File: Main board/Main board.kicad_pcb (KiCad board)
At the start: 2 copper layers, 126 x 88.5 mm, 35 parts

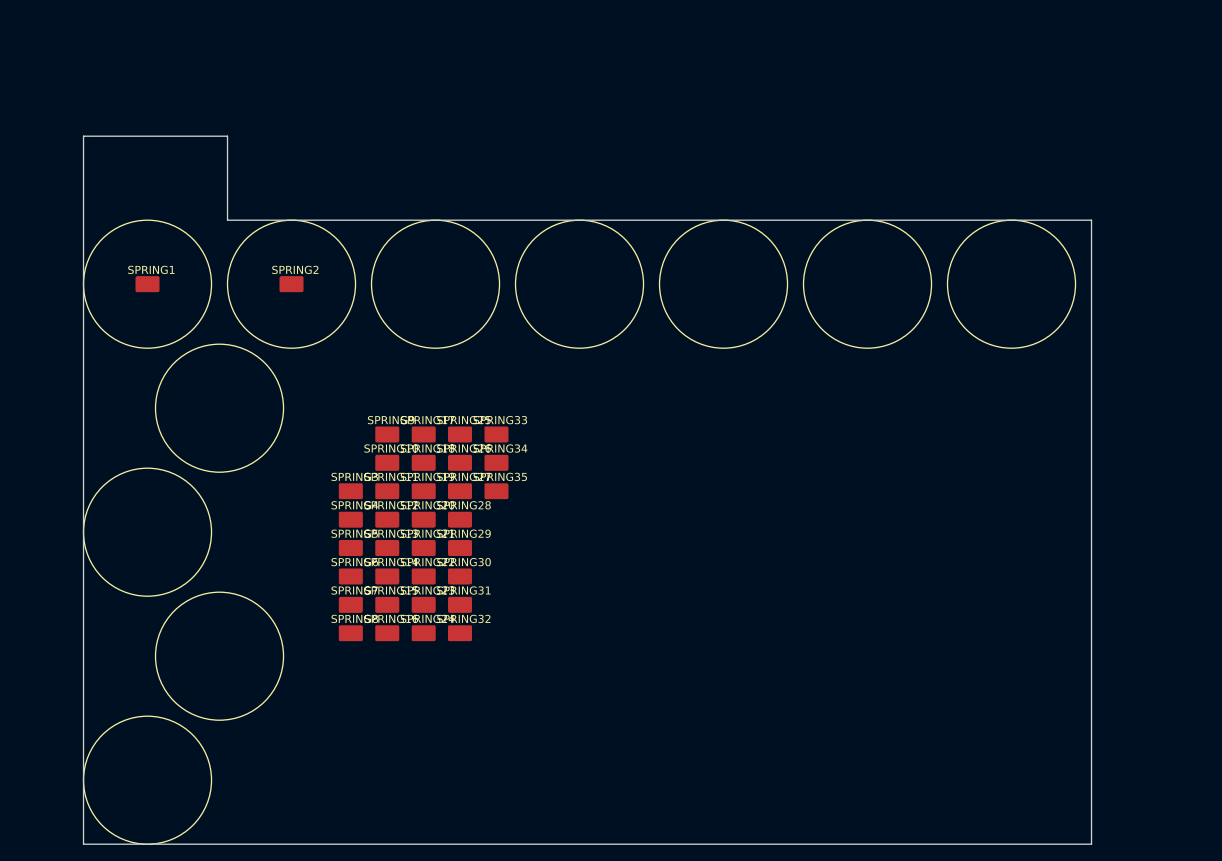
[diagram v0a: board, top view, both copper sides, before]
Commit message: Created breakable symmetrical version
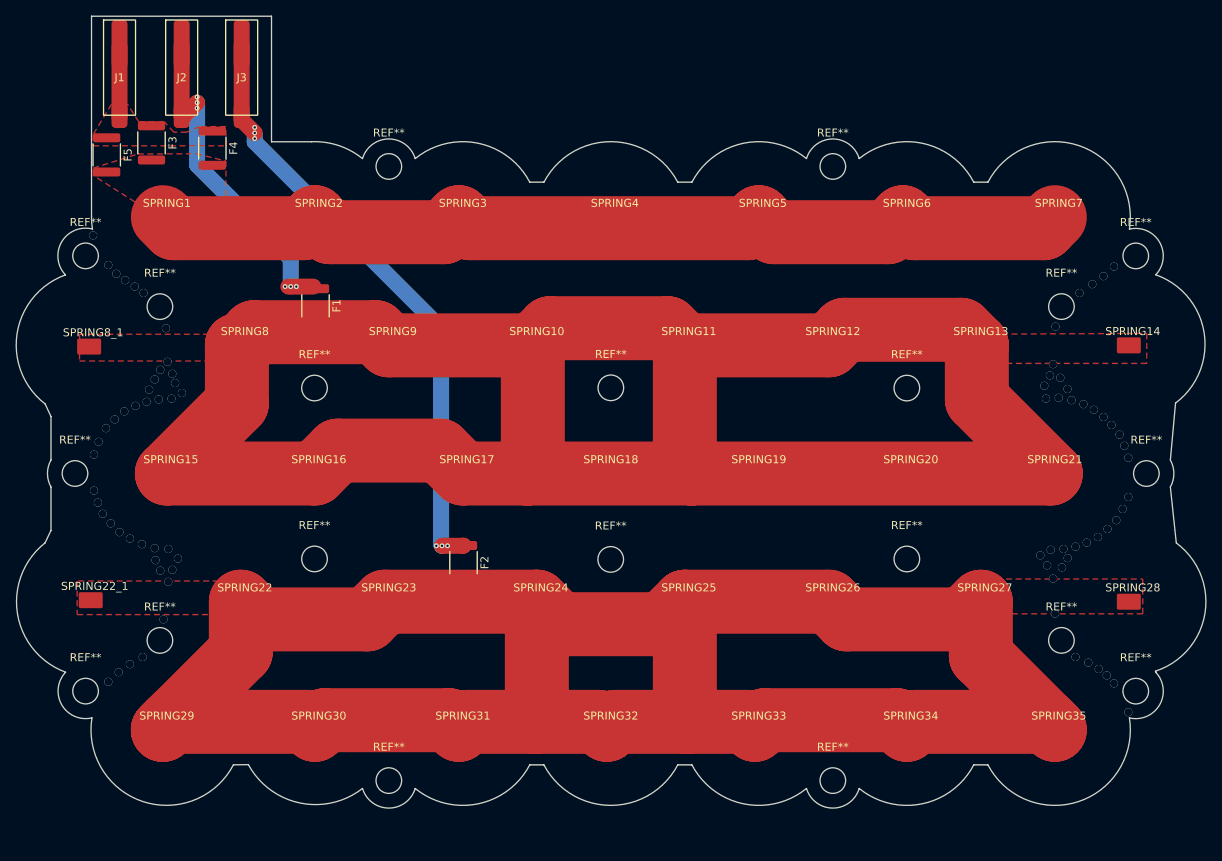
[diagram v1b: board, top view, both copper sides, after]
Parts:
- added F1: Polyfuse, Fuse:Fuse_1812_4532Metric, F.Cu at (41.0, 33.2)
- added F2: Polyfuse, Fuse:Fuse_1812_4532Metric, F.Cu at (59.5, 65.3)
- added F3: Polyfuse, Fuse:Fuse_1812_4532Metric, F.Cu at (20.5, 12.8)
- added F4: Polyfuse, Fuse:Fuse_1812_4532Metric, F.Cu at (28.1, 13.5)
- added F5: Polyfuse, Fuse:Fuse_1812_4532Metric, F.Cu at (14.9, 14.3)
- added J1: Conn_01x01_Pin, SMD_spring_clamp_connector:SMD_spring_clamp_connector_1x1, F.Cu at (16.5, 9.38)
- added J2: Conn_01x01_Pin, SMD_spring_clamp_connector:SMD_spring_clamp_connector_1x1, F.Cu at (24.3, 9.38)
- added J3: Conn_01x01_Pin, SMD_spring_clamp_connector:SMD_spring_clamp_connector_1x1, F.Cu at (31.8, 9.38)
- added REF**: MountingHole_3.2mm_M3, MountingHole:MountingHole_3.2mm_M3, F.Cu at (21.5, 33.3)
- added REF**: MountingHole_3.2mm_M3, MountingHole:MountingHole_3.2mm_M3, F.Cu at (77.9, 64.9)
- added REF**: MountingHole_3.2mm_M3, MountingHole:MountingHole_3.2mm_M3, F.Cu at (77.9, 43.5)
- added REF**: MountingHole_3.2mm_M3, MountingHole:MountingHole_3.2mm_M3, F.Cu at (50.2, 15.8)
- added REF**: MountingHole_3.2mm_M3, MountingHole:MountingHole_3.2mm_M3, F.Cu at (134.2, 75.0)
- added REF**: MountingHole_3.2mm_M3, MountingHole:MountingHole_3.2mm_M3, F.Cu at (12.3, 27.0)
- added REF**: MountingHole_3.2mm_M3, MountingHole:MountingHole_3.2mm_M3, F.Cu at (144.9, 54.2)
- added REF**: MountingHole_3.2mm_M3, MountingHole:MountingHole_3.2mm_M3, F.Cu at (114.9, 43.5)
- added REF**: MountingHole_3.2mm_M3, MountingHole:MountingHole_3.2mm_M3, F.Cu at (40.9, 43.5)
- added REF**: MountingHole_3.2mm_M3, MountingHole:MountingHole_3.2mm_M3, F.Cu at (21.5, 75.0)
- added REF**: MountingHole_3.2mm_M3, MountingHole:MountingHole_3.2mm_M3, F.Cu at (10.9, 54.2)
- added REF**: MountingHole_3.2mm_M3, MountingHole:MountingHole_3.2mm_M3, F.Cu at (50.2, 92.5)
- added REF**: MountingHole_3.2mm_M3, MountingHole:MountingHole_3.2mm_M3, F.Cu at (105.7, 15.8)
- added REF**: MountingHole_3.2mm_M3, MountingHole:MountingHole_3.2mm_M3, F.Cu at (134.2, 33.3)
- added REF**: MountingHole_3.2mm_M3, MountingHole:MountingHole_3.2mm_M3, F.Cu at (12.3, 81.4)
- added REF**: MountingHole_3.2mm_M3, MountingHole:MountingHole_3.2mm_M3, F.Cu at (143.5, 27.0)
- added REF**: MountingHole_3.2mm_M3, MountingHole:MountingHole_3.2mm_M3, F.Cu at (114.9, 64.8)
- added REF**: MountingHole_3.2mm_M3, MountingHole:MountingHole_3.2mm_M3, F.Cu at (105.7, 92.5)
- added REF**: MountingHole_3.2mm_M3, MountingHole:MountingHole_3.2mm_M3, F.Cu at (143.5, 81.4)
- added REF**: MountingHole_3.2mm_M3, MountingHole:MountingHole_3.2mm_M3, F.Cu at (40.9, 64.8)
- added SPRING22_1: spring_tab, spring_tab:spring_tab, F.Cu at (13.4, 70.0)
- added SPRING8_1: spring_tab, spring_tab:spring_tab, F.Cu at (13.2, 38.3)
- moved SPRING7 100.5 mm to (133.9, 22.1)
- moved SPRING14 97.1 mm to (143.2, 38.1)
- moved SPRING28 84.2 mm to (143.2, 70.2)
- moved SPRING6 82.3 mm to (114.9, 22.1)
- moved SPRING21 79.0 mm to (133.4, 54.2)
- moved SPRING13 77.9 mm to (124.2, 38.1)
- moved SPRING35 75.9 mm to (133.9, 86.2)
- moved SPRING27 66.6 mm to (124.7, 70.2)
- moved SPRING5 65.7 mm to (96.9, 22.1)
- moved SPRING34 61.2 mm to (115.4, 86.2)
- moved SPRING20 60.7 mm to (115.4, 54.2)
- moved SPRING12 59.3 mm to (105.7, 38.1)
- moved SPRING4 49.9 mm to (78.4, 22.1)
- moved SPRING26 49.3 mm to (105.7, 70.2)
- moved SPRING33 49.1 mm to (96.4, 86.2)
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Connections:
- SPRING16 pad 1: Net-(F2-Pad2) -> Net-(F1-Pad2)
- SPRING18 pad 1: Net-(F2-Pad2) -> Net-(F1-Pad2)
- SPRING20 pad 1: Net-(F2-Pad2) -> Net-(F1-Pad2)
- SPRING23 pad 1: Net-(F1-Pad2) -> Net-(F2-Pad2)
- SPRING25 pad 1: Net-(F1-Pad2) -> Net-(F2-Pad2)
- SPRING27 pad 1: Net-(F1-Pad2) -> Net-(F2-Pad2)
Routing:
- net Net-(F2-Pad2): track 0.00 -> 288.0 mm
- net Net-(F1-Pad2): track 0.00 -> 282.5 mm
- net Net-(F3-Pad2): track 0.00 -> 118.0 mm
- net Net-(J3-Pin_1): track 0.00 -> 76.1 mm, vias 0 -> 6
- net Net-(J2-Pin_1): track 0.00 -> 42.6 mm, vias 0 -> 6
- net Net-(J1-Pin_1): track 0.00 -> 9.00 mm
- net (no net): vias 0 -> 83
- added copper zone on F.Cu, net Net-(F1-Pad2)
- added copper zone on F.Cu, net Net-(F2-Pad2)
- added copper zone on F.Cu, net Net-(F3-Pad2)
- added copper zone on F.Cu, net Net-(J1-Pin_1)
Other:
- board size 126 x 88.5 mm -> 148.7 x 99 mm
